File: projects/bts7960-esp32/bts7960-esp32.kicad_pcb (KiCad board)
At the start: 2 copper layers, 10 parts, among them J1 CONN_02X04, J2 CONN_01X04, U1 ESP32-DEVKIT-V1

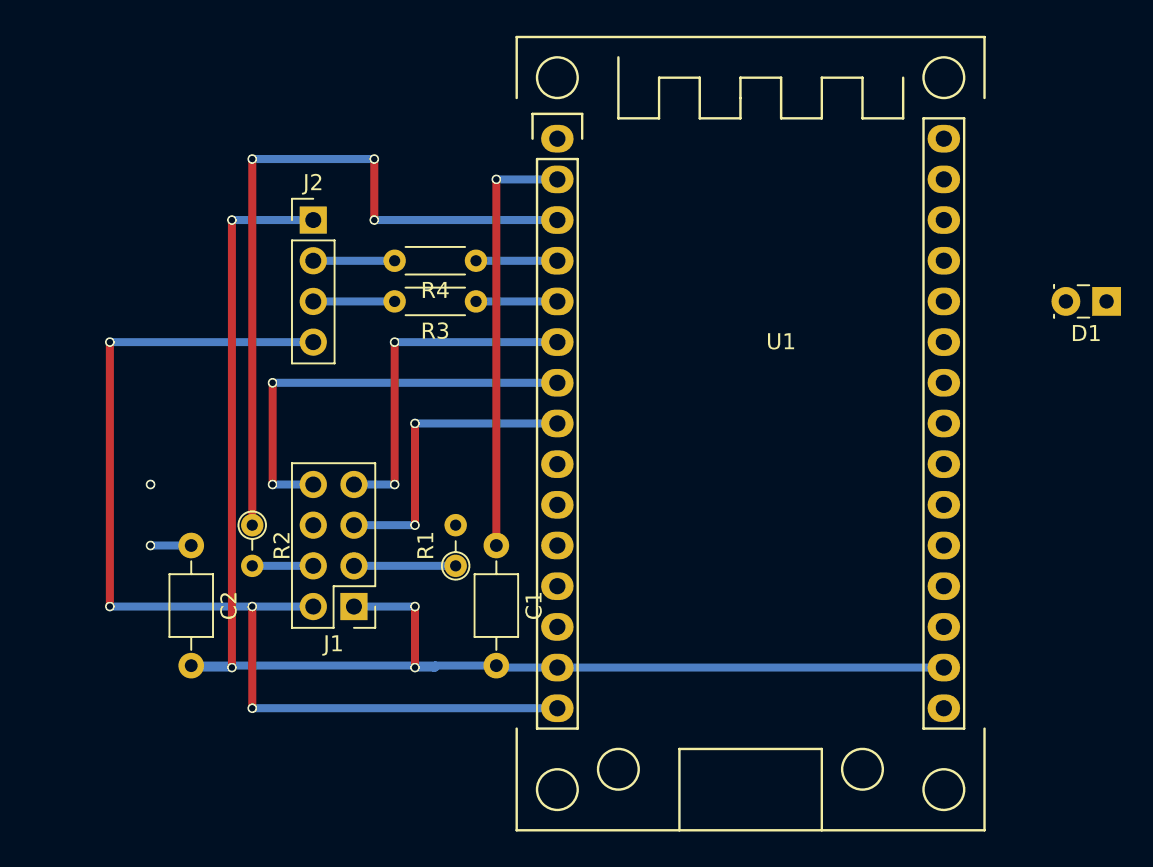
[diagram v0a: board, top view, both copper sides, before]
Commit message: working on universal esp32 board
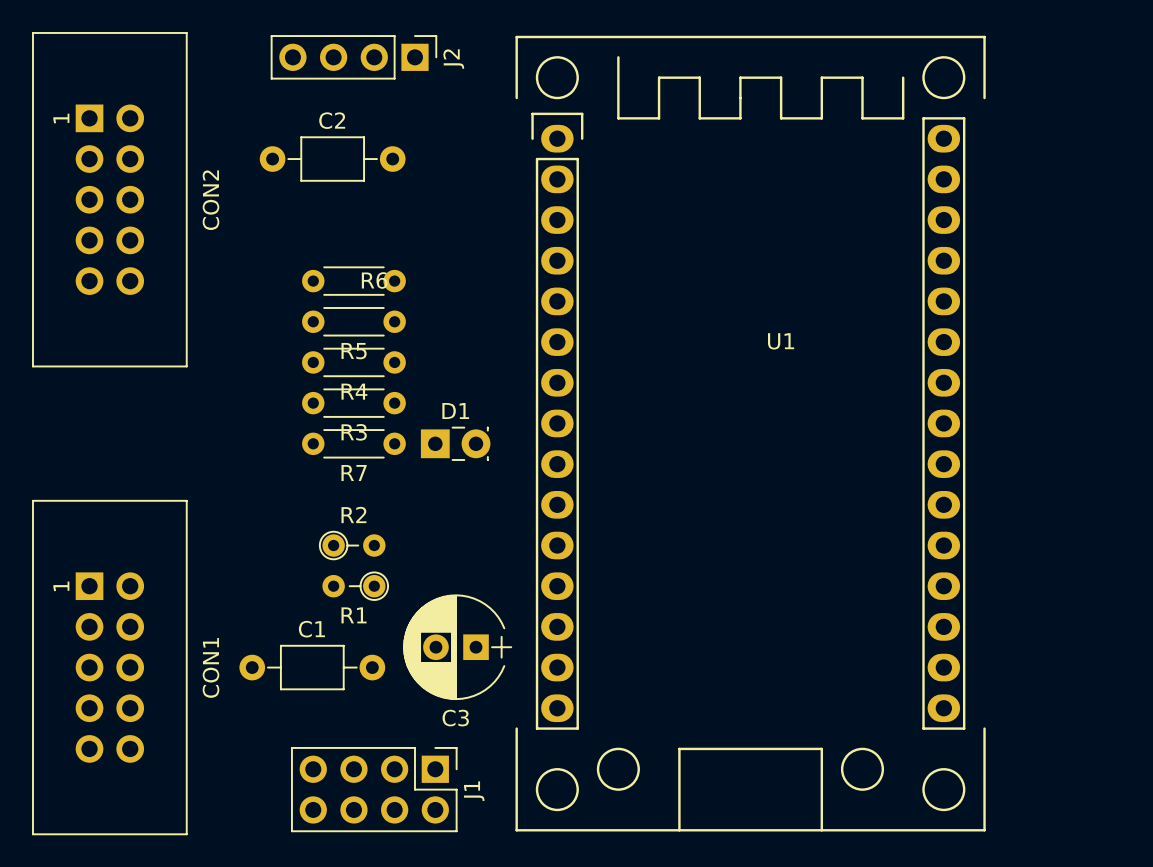
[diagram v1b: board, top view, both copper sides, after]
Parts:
- added C3: CP, Capacitors_THT:CP_Radial_D6.3mm_P2.50mm, F.Cu at (167.6, 129.5)
- added CON1: UEXT-5V, limero-lib:UEXT, F.Cu at (143.5, 125.7)
- added CON2: UEXT-5V, limero-lib:UEXT, F.Cu at (143.5, 96.5)
- added R5: 10K, Resistors_THT:R_Axial_DIN0204_L3.6mm_D1.6mm_P5.08mm_Horizontal, F.Cu at (162.6, 109.2)
- added R6: 10K, Resistors_THT:R_Axial_DIN0204_L3.6mm_D1.6mm_P5.08mm_Horizontal, F.Cu at (162.6, 106.7)
- added R7: R, Resistors_THT:R_Axial_DIN0204_L3.6mm_D1.6mm_P5.08mm_Horizontal, F.Cu at (162.6, 116.8)
- C1, C2: value C_Small -> 0.1µ
- R1, R2, R3, R4: value R -> 10k
- moved D1 42.8 mm to (165.1, 116.8), turned to 0 degrees
- moved C2 24.7 mm to (154.9, 99.1), turned to 0 degrees
- moved C1 17.0 mm to (153.7, 130.8), turned to 0 degrees
- moved J2 12.0 mm to (163.8, 92.7), turned to 270 degrees
- moved J1 11.4 mm to (165.1, 137.2), turned to 270 degrees
- moved R4 8.13 mm to (162.6, 111.8)
- moved R3 8.13 mm to (162.6, 114.3)
- moved R1 5.24 mm to (161.3, 125.7), turned to 180 degrees
- moved R2 5.24 mm to (158.8, 123.2), turned to 0 degrees
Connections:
- net MISO1 renamed CHAN_A
- net MISO2 renamed CHAN_B
- net RXD1 renamed L_IS
- net SCL1 renamed L_EN
- net SDA1 renamed R_EN
- net SSEL1 renamed R_PWM
- net SSEL2 renamed L_PWM
- C2 pad 2: GND -> (no net)
- D1 pad 1: (no net) -> Net-(D1-Pad1)
- D1 pad 2: Net-(D1-Pad2) -> (no net)
- U1 pad 10: (no net) -> SCL2
- U1 pad 11: (no net) -> SDA2
- U1 pad 21: (no net) -> SCK2
- U1 pad 22: (no net) -> SCK1
- U1 pad 24: (no net) -> TXD2
- U1 pad 25: (no net) -> TXD1
- U1 pad 26: Net-(D1-Pad2) -> (no net)
- U1 pad 29: (no net) -> MOSI2
- U1 pad 30: (no net) -> MOSI1
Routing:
- net GND: track 91.8 -> 0.00 mm, vias 4 -> 0
- net 5V: track 67.3 -> 0.00 mm, vias 4 -> 0
- net RXD2: track 48.3 -> 0.00 mm, vias 5 -> 0
- net L_IS: track 26.7 -> 0.00 mm, vias 1 -> 0
- net R_PWM: track 26.7 -> 0.00 mm, vias 2 -> 0
- net L_PWM: track 21.6 -> 0.00 mm, vias 2 -> 0
- net L_EN: track 19.0 -> 0.00 mm, vias 2 -> 0
- net Net-(J1-Pad3): track 6.35 -> 0.00 mm
- net Net-(J2-Pad3): track 5.08 -> 0.00 mm
- net Net-(J2-Pad2): track 5.08 -> 0.00 mm
- net CHAN_B: track 5.08 -> 0.00 mm
- net CHAN_A: track 5.08 -> 0.00 mm
- net Net-(J1-Pad4): track 3.81 -> 0.00 mm
